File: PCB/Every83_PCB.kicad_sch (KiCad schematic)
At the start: 33 parts, among them J1 781710004, J2 Conn_01x08_Socket, J3 SM03B-SRSS-TB, J4 SM03B-SRSS-TB, J5 Conn_01x08_Socket, Q3 DMG2305, SW101 KMR2, SW102 KMR2, U1 Core52840, U2 AP2112(3.3V)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

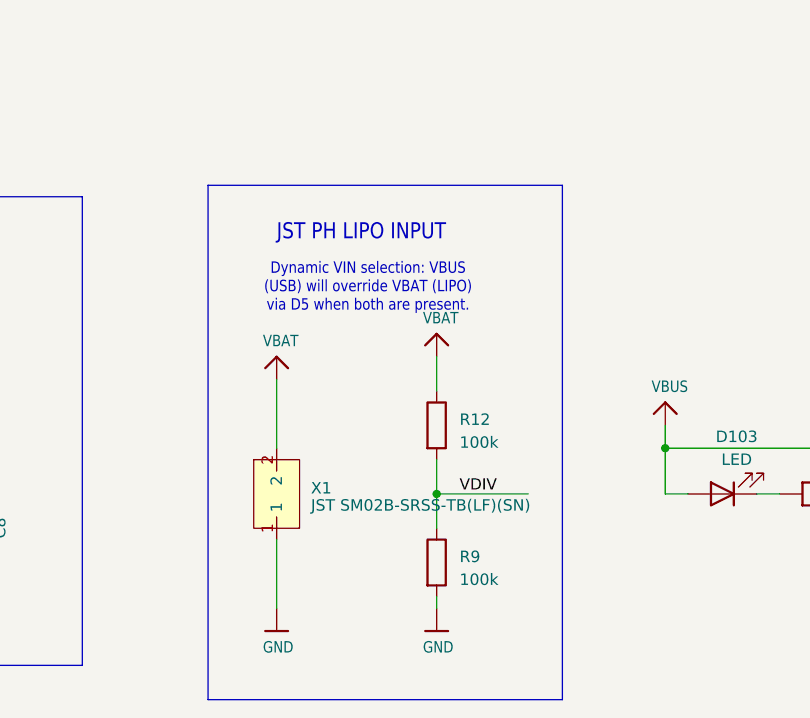
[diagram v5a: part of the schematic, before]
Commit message: add power switch
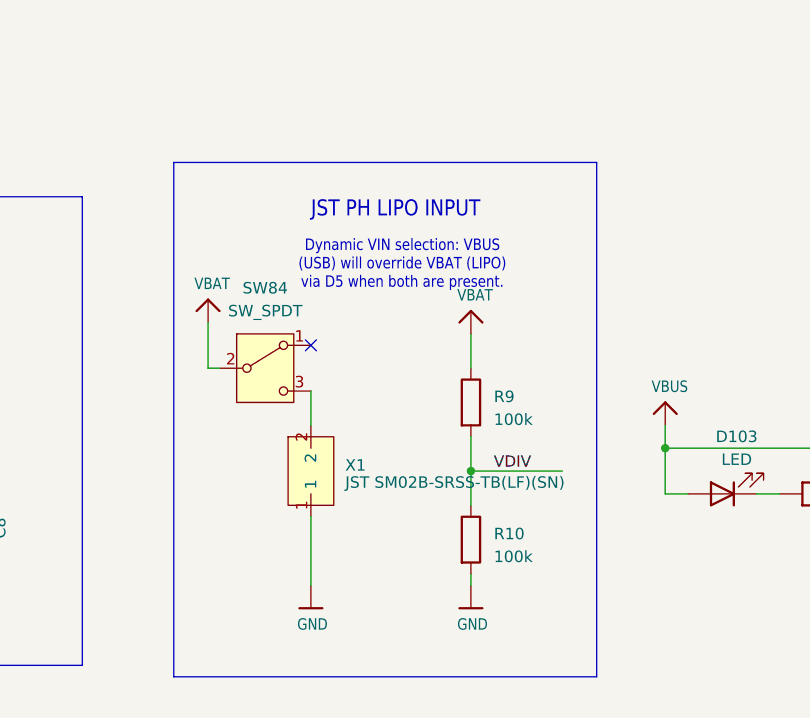
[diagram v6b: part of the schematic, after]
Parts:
- removed R12: 100k, Resistor_SMD:R_0603_1608Metric, symbol Device:R
- added R10: 100k, Resistor_SMD:R_0603_1608Metric, symbol Device:R
- added SW84: SW_SPDT, JohnDeereLibrary:ET01M3D1SA1BE, symbol Switch:SW_SPDT
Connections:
- net GND: now also R10.2; no longer R9.2
- net VBAT: now also R9.1, SW84.2 (B); no longer X1.2
- net VDIV: now also R9.2, R10.1; no longer R9.1
- new net: SW84.3 (C), X1.2
- no-connect marks 0 -> 1

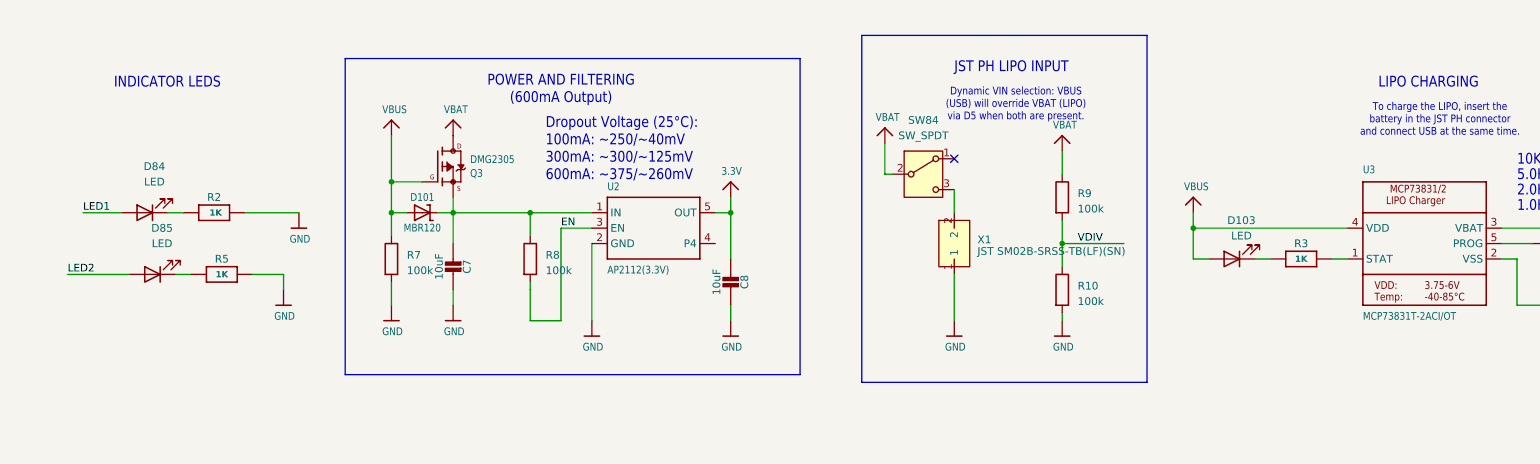
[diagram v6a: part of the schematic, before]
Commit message: small changes to UX for charging
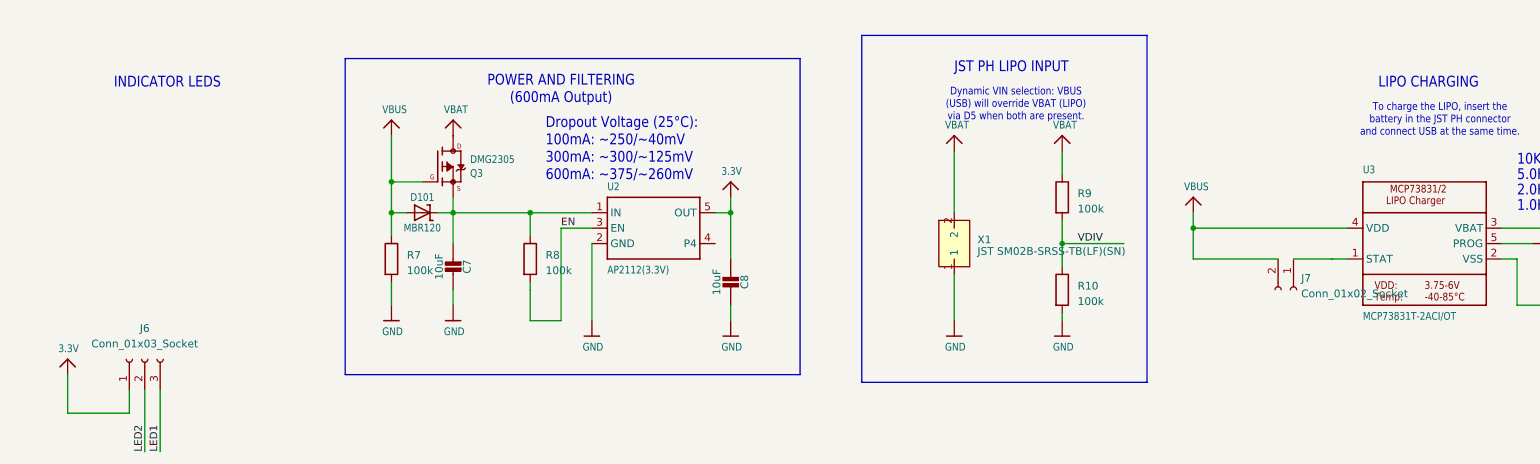
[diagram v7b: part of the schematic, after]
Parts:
- removed D103: LED, Diode_SMD:D_0805_2012Metric_Pad1.15x1.40mm_HandSolder, symbol Device:LED
- removed D84, D85: LED, LED_SMD:LED_0805_2012Metric, symbol Device:LED
- removed R2, R3, R5: 1K, Resistor_SMD:R_0603_1608Metric, symbol Adafruit nRF52840 Bluefruit Feather Express Rev D-eagle-import:RESISTOR_0603_NO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
- removed SW84: SW_SPDT, JohnDeereLibrary:ET01M3D1SA1BE, symbol Switch:SW_SPDT
- added J6: Conn_01x03_Socket, symbol Connector:Conn_01x03_Socket
- added J7: Conn_01x02_Socket, symbol Connector:Conn_01x02_Socket
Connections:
- net 3.3V: now also J6.1 (Pin_1)
- net LED1: now also J6.3 (Pin_3)
- net LED2: now also J6.2 (Pin_2)
- net VBAT: now also X1.2
- net VBUS: now also J7.2 (Pin_2)
- net at U3.1 (STAT): now also J7.1 (Pin_1)
- no-connect marks 1 -> 0
